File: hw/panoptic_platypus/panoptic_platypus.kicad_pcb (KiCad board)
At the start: 2 copper layers, 127.4 x 73 mm, 206 parts, among them J1 Conn_Coaxial, J2 Conn_Coaxial, J3 Conn_Coaxial, J4 Conn_Coaxial, T1 MABA-011082, T2 MABA-011082, T3 MABA-011082, T4 MABA-011082, U1 MAX2851, U10 ECP5_5G_25_CABGA381, U2 LTC5510, U3 LTC5510, U4 LTC5510, U5 LTC5510, U6 AD9268, U7 AD9268, U8 AD9268, U9 AD9268

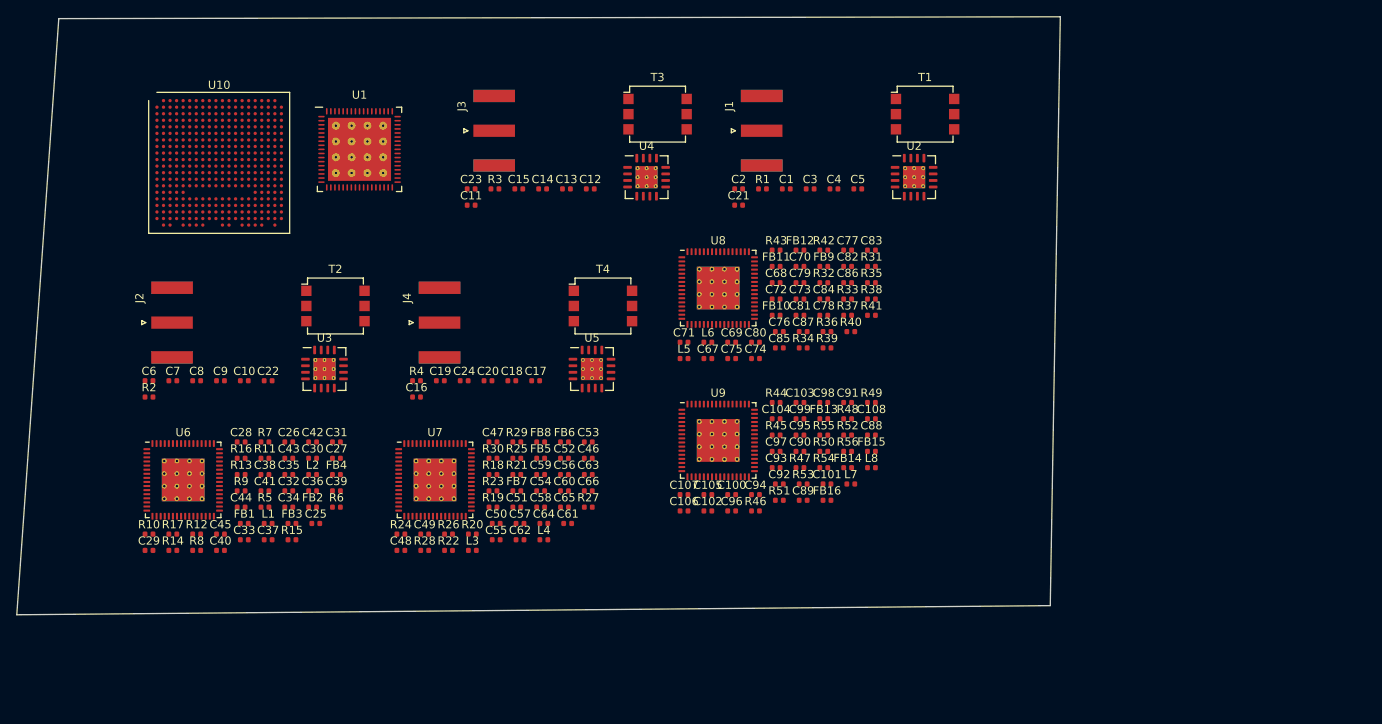
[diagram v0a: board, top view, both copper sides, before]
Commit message: Added LO Generator, fixed some smybols
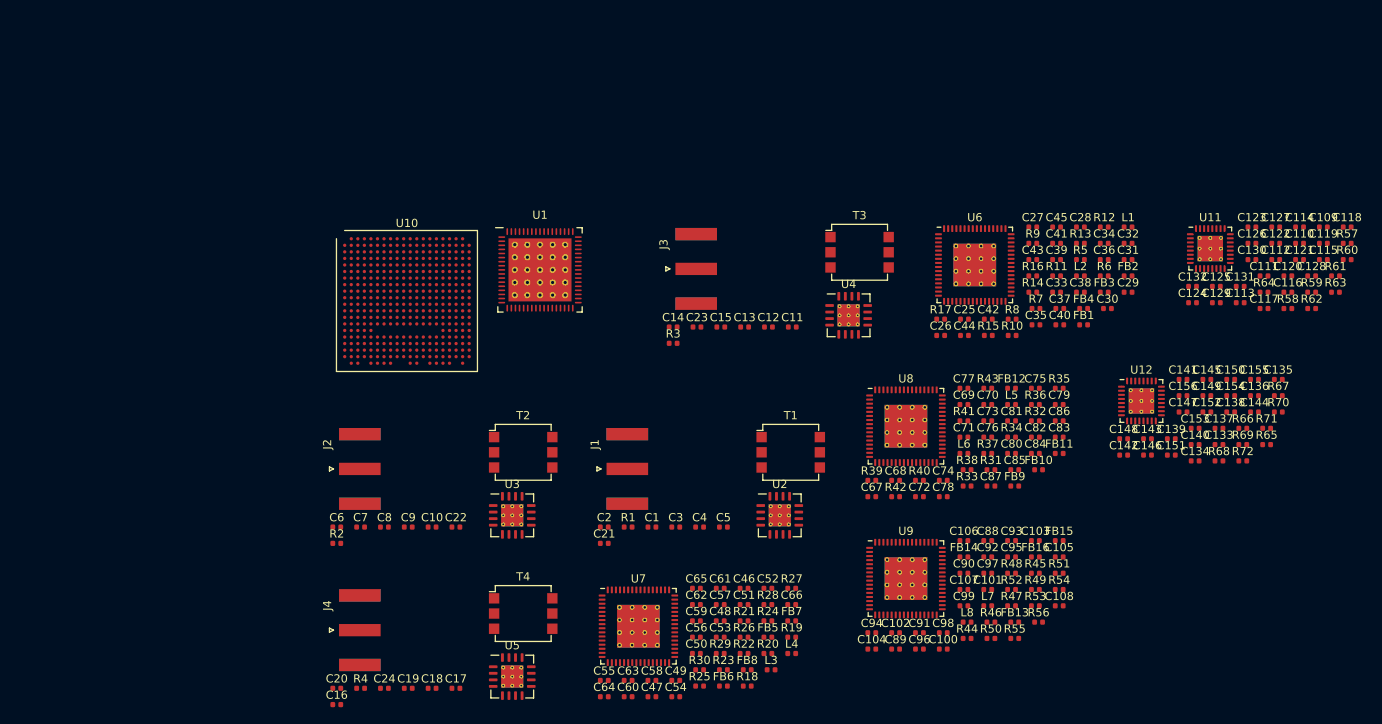
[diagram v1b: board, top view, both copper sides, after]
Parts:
- added C109: 100p, Capacitor_SMD:C_0402_1005Metric, F.Cu at (210.1, 70.8)
- added C110: 100p, Capacitor_SMD:C_0402_1005Metric, F.Cu at (207.2, 72.8)
- added C111: 100p, Capacitor_SMD:C_0402_1005Metric, F.Cu at (202.9, 76.8)
- added C112: 100p, Capacitor_SMD:C_0402_1005Metric, F.Cu at (204.3, 74.8)
- added C113: 0.01u, Capacitor_SMD:C_0402_1005Metric, F.Cu at (200.0, 80.0)
- added C114: 0.01u, Capacitor_SMD:C_0402_1005Metric, F.Cu at (207.2, 70.8)
- added C115: 0.1u, Capacitor_SMD:C_0402_1005Metric, F.Cu at (210.1, 74.8)
- added C116: 100p, Capacitor_SMD:C_0402_1005Metric, F.Cu at (205.8, 78.8)
- added C117: 1u, Capacitor_SMD:C_0402_1005Metric, F.Cu at (202.9, 80.8)
- added C118: 0.1u, Capacitor_SMD:C_0402_1005Metric, F.Cu at (213.0, 70.8)
- added C119: 1u, Capacitor_SMD:C_0402_1005Metric, F.Cu at (210.1, 72.8)
- added C120: 820p, Capacitor_SMD:C_0402_1005Metric, F.Cu at (205.8, 76.8)
- added C121: 100p, Capacitor_SMD:C_0402_1005Metric, F.Cu at (207.2, 74.8)
- added C122: 0.1u, Capacitor_SMD:C_0402_1005Metric, F.Cu at (204.3, 72.8)
- added C123: 0.012u, Capacitor_SMD:C_0402_1005Metric, F.Cu at (201.4, 70.8)
- added C124: 0.1u, Capacitor_SMD:C_0402_1005Metric, F.Cu at (194.1, 80.0)
- added C125: 100p, Capacitor_SMD:C_0402_1005Metric, F.Cu at (197.0, 78.1)
- added C126: 1u, Capacitor_SMD:C_0402_1005Metric, F.Cu at (201.4, 72.8)
- added C127: 0.1u, Capacitor_SMD:C_0402_1005Metric, F.Cu at (204.3, 70.8)
- added C128: 100p, Capacitor_SMD:C_0402_1005Metric, F.Cu at (208.7, 76.8)
- added C129: 0.1u, Capacitor_SMD:C_0402_1005Metric, F.Cu at (197.0, 80.0)
- added C130: 100p, Capacitor_SMD:C_0402_1005Metric, F.Cu at (201.4, 74.8)
- added C131: 0.1u, Capacitor_SMD:C_0402_1005Metric, F.Cu at (200.0, 78.1)
- added C132: 100p, Capacitor_SMD:C_0402_1005Metric, F.Cu at (194.1, 78.1)
- added C133: 100p, Capacitor_SMD:C_0402_1005Metric, F.Cu at (197.4, 97.4)
- added C134: 100p, Capacitor_SMD:C_0402_1005Metric, F.Cu at (194.5, 99.4)
- added C135: 100p, Capacitor_SMD:C_0402_1005Metric, F.Cu at (204.6, 89.4)
- added C136: 100p, Capacitor_SMD:C_0402_1005Metric, F.Cu at (201.7, 91.4)
- added C137: 0.01u, Capacitor_SMD:C_0402_1005Metric, F.Cu at (197.4, 95.4)
- added C138: 0.01u, Capacitor_SMD:C_0402_1005Metric, F.Cu at (198.8, 93.4)
- added C139: 0.1u, Capacitor_SMD:C_0402_1005Metric, F.Cu at (191.5, 96.7)
- added C140: 100p, Capacitor_SMD:C_0402_1005Metric, F.Cu at (194.5, 97.4)
- added C141: 1u, Capacitor_SMD:C_0402_1005Metric, F.Cu at (193.0, 89.4)
- added C142: 0.1u, Capacitor_SMD:C_0402_1005Metric, F.Cu at (185.7, 98.7)
- added C143: 1u, Capacitor_SMD:C_0402_1005Metric, F.Cu at (188.6, 96.7)
- added C144: 820p, Capacitor_SMD:C_0402_1005Metric, F.Cu at (201.7, 93.4)
- added C145: 100p, Capacitor_SMD:C_0402_1005Metric, F.Cu at (195.9, 89.4)
- added C146: 0.1u, Capacitor_SMD:C_0402_1005Metric, F.Cu at (188.6, 98.7)
- added C147: 0.012u, Capacitor_SMD:C_0402_1005Metric, F.Cu at (193.0, 93.4)
- added C148: 0.1u, Capacitor_SMD:C_0402_1005Metric, F.Cu at (185.7, 96.7)
- added C149: 100p, Capacitor_SMD:C_0402_1005Metric, F.Cu at (195.9, 91.4)
- added C150: 1u, Capacitor_SMD:C_0402_1005Metric, F.Cu at (198.8, 89.4)
- added C151: 0.1u, Capacitor_SMD:C_0402_1005Metric, F.Cu at (191.5, 98.7)
- added C152: 100p, Capacitor_SMD:C_0402_1005Metric, F.Cu at (195.9, 93.4)
- added C153: 0.1u, Capacitor_SMD:C_0402_1005Metric, F.Cu at (194.5, 95.4)
- added C154: 100p, Capacitor_SMD:C_0402_1005Metric, F.Cu at (198.8, 91.4)
- added C155: 0.1u, Capacitor_SMD:C_0402_1005Metric, F.Cu at (201.7, 89.4)
- added C156: 100p, Capacitor_SMD:C_0402_1005Metric, F.Cu at (193.0, 91.4)
- added R57: 50, Resistor_SMD:R_0402_1005Metric, F.Cu at (213.0, 72.8)
- added R58: 50, Resistor_SMD:R_0402_1005Metric, F.Cu at (205.8, 80.8)
- added R59: 50, Resistor_SMD:R_0402_1005Metric, F.Cu at (208.7, 78.8)
- added R60: 50, Resistor_SMD:R_0402_1005Metric, F.Cu at (213.0, 74.8)
- added R61: 90.9, Resistor_SMD:R_0402_1005Metric, F.Cu at (211.6, 76.8)
- added R62: 30.1, Resistor_SMD:R_0402_1005Metric, F.Cu at (208.7, 80.8)
- added R63: 240, Resistor_SMD:R_0402_1005Metric, F.Cu at (211.6, 78.8)
- added R64: 5.1k, Resistor_SMD:R_0402_1005Metric, F.Cu at (202.9, 78.8)
- added R65: 50, Resistor_SMD:R_0402_1005Metric, F.Cu at (203.2, 97.4)
- added R66: 50, Resistor_SMD:R_0402_1005Metric, F.Cu at (200.3, 95.4)
- added R67: 50, Resistor_SMD:R_0402_1005Metric, F.Cu at (204.6, 91.4)
- added R68: 50, Resistor_SMD:R_0402_1005Metric, F.Cu at (197.4, 99.4)
- added R69: 90.9, Resistor_SMD:R_0402_1005Metric, F.Cu at (200.3, 97.4)
- added R70: 30.1, Resistor_SMD:R_0402_1005Metric, F.Cu at (204.6, 93.4)
- added R71: 240, Resistor_SMD:R_0402_1005Metric, F.Cu at (203.2, 95.4)
- added R72: 5.1k, Resistor_SMD:R_0402_1005Metric, F.Cu at (200.3, 99.4)
- added U11: MAX2871, Package_DFN_QFN:TQFN-32-1EP_5x5mm_P0.5mm_EP3.1x3.1mm_ThermalVias, F.Cu at (196.3, 73.4)
- added U12: MAX2871, Package_DFN_QFN:TQFN-32-1EP_5x5mm_P0.5mm_EP3.1x3.1mm_ThermalVias, F.Cu at (187.9, 92.0)
- U1: footprint dknueppe:TQFN-68_EP_10x10_Pitch0.5mm -> dknueppe:TQFN-68_EP_10x10_Pitch0.5mm_EP7.7mmx7.7mm_ThermalVias
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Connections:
- net /Analog_Backend/CLK+ renamed /ADC Path2/CLK+
- net /Analog_Backend/CLK- renamed /ADC Path2/CLK-
- net /Analog_Backend/CSB renamed /ADC Path2/CSB
- net /Analog_Backend/DCO_I renamed /ADC Path2/DCO_I
- net /Analog_Backend/DCO_Q renamed /ADC Path2/DCO_Q
- net /Analog_Backend/I_IN+ renamed /ADC Path2/I_IN+
- net /Analog_Backend/I_IN- renamed /ADC Path2/I_IN-
- net /Analog_Backend/I_OUT0 renamed /ADC Path2/I_OUT0
- net /Analog_Backend/I_OUT1 renamed /ADC Path2/I_OUT1
- net /Analog_Backend/I_OUT10 renamed /ADC Path2/I_OUT10
- net /Analog_Backend/I_OUT11 renamed /ADC Path2/I_OUT11
- net /Analog_Backend/I_OUT12 renamed /ADC Path2/I_OUT12
- net /Analog_Backend/I_OUT13 renamed /ADC Path2/I_OUT13
- net /Analog_Backend/I_OUT14 renamed /ADC Path2/I_OUT14
- net /Analog_Backend/I_OUT15 renamed /ADC Path2/I_OUT15
- net /Analog_Backend/I_OUT2 renamed /ADC Path2/I_OUT2
- net /Analog_Backend/I_OUT3 renamed /ADC Path2/I_OUT3
- net /Analog_Backend/I_OUT4 renamed /ADC Path2/I_OUT4
- net /Analog_Backend/I_OUT5 renamed /ADC Path2/I_OUT5
- net /Analog_Backend/I_OUT6 renamed /ADC Path2/I_OUT6
- net /Analog_Backend/I_OUT7 renamed /ADC Path2/I_OUT7
- net /Analog_Backend/I_OUT8 renamed /ADC Path2/I_OUT8
- net /Analog_Backend/I_OUT9 renamed /ADC Path2/I_OUT9
- net /Analog_Backend/OEB renamed /ADC Path2/OEB
- net /Analog_Backend/OR_I renamed /ADC Path2/OR_I
- net /Analog_Backend/OR_Q renamed /ADC Path2/OR_Q
- net /Analog_Backend/PDWN renamed /ADC Path2/PDWN
- net /Analog_Backend/Q_IN+ renamed /ADC Path2/Q_IN+
- net /Analog_Backend/Q_IN- renamed /ADC Path2/Q_IN-
- net /Analog_Backend/Q_OUT0 renamed /ADC Path2/Q_OUT0
- net /Analog_Backend/Q_OUT1 renamed /ADC Path2/Q_OUT1
- net /Analog_Backend/Q_OUT10 renamed /ADC Path2/Q_OUT10
- net /Analog_Backend/Q_OUT11 renamed /ADC Path2/Q_OUT11
- net /Analog_Backend/Q_OUT12 renamed /ADC Path2/Q_OUT12
- net /Analog_Backend/Q_OUT13 renamed /ADC Path2/Q_OUT13
- net /Analog_Backend/Q_OUT14 renamed /ADC Path2/Q_OUT14
- net /Analog_Backend/Q_OUT15 renamed /ADC Path2/Q_OUT15
- net /Analog_Backend/Q_OUT2 renamed /ADC Path2/Q_OUT2
- net /Analog_Backend/Q_OUT3 renamed /ADC Path2/Q_OUT3
- net /Analog_Backend/Q_OUT4 renamed /ADC Path2/Q_OUT4
- net /Analog_Backend/Q_OUT5 renamed /ADC Path2/Q_OUT5
- net /Analog_Backend/Q_OUT6 renamed /ADC Path2/Q_OUT6
- net /Analog_Backend/Q_OUT7 renamed /ADC Path2/Q_OUT7
- net /Analog_Backend/Q_OUT8 renamed /ADC Path2/Q_OUT8
- net /Analog_Backend/Q_OUT9 renamed /ADC Path2/Q_OUT9
- net /Analog_Backend/SCLK renamed /ADC Path2/SCLK
- net /Analog_Backend/SDIO renamed /ADC Path2/SDIO
- net /Analog_Backend/SYNC renamed /ADC Path2/SYNC
- net /sheet5F973422/CLK+ renamed /ADC Path 3/CLK+
- net /sheet5F973422/CLK- renamed /ADC Path 3/CLK-
- net /sheet5F973422/CSB renamed /ADC Path 3/CSB
- net /sheet5F973422/DCO_I renamed /ADC Path 3/DCO_I
- net /sheet5F973422/DCO_Q renamed /ADC Path 3/DCO_Q
- net /sheet5F973422/I_IN+ renamed /ADC Path 3/I_IN+
- net /sheet5F973422/I_IN- renamed /ADC Path 3/I_IN-
- net /sheet5F973422/I_OUT0 renamed /ADC Path 3/I_OUT0
- net /sheet5F973422/I_OUT1 renamed /ADC Path 3/I_OUT1
- net /sheet5F973422/I_OUT10 renamed /ADC Path 3/I_OUT10
- net /sheet5F973422/I_OUT11 renamed /ADC Path 3/I_OUT11
- net /sheet5F973422/I_OUT12 renamed /ADC Path 3/I_OUT12
- net /sheet5F973422/I_OUT13 renamed /ADC Path 3/I_OUT13
- net /sheet5F973422/I_OUT14 renamed /ADC Path 3/I_OUT14
- net /sheet5F973422/I_OUT15 renamed /ADC Path 3/I_OUT15
- net /sheet5F973422/I_OUT2 renamed /ADC Path 3/I_OUT2
- net /sheet5F973422/I_OUT3 renamed /ADC Path 3/I_OUT3
- net /sheet5F973422/I_OUT4 renamed /ADC Path 3/I_OUT4
- net /sheet5F973422/I_OUT5 renamed /ADC Path 3/I_OUT5
- net /sheet5F973422/I_OUT6 renamed /ADC Path 3/I_OUT6
- net /sheet5F973422/I_OUT7 renamed /ADC Path 3/I_OUT7
- net /sheet5F973422/I_OUT8 renamed /ADC Path 3/I_OUT8
- net /sheet5F973422/I_OUT9 renamed /ADC Path 3/I_OUT9
- net /sheet5F973422/OEB renamed /ADC Path 3/OEB
- net /sheet5F973422/OR_I renamed /ADC Path 3/OR_I
- net /sheet5F973422/OR_Q renamed /ADC Path 3/OR_Q
- net /sheet5F973422/PDWN renamed /ADC Path 3/PDWN
- net /sheet5F973422/Q_IN+ renamed /ADC Path 3/Q_IN+
- net /sheet5F973422/Q_IN- renamed /ADC Path 3/Q_IN-
- net /sheet5F973422/Q_OUT0 renamed /ADC Path 3/Q_OUT0
- net /sheet5F973422/Q_OUT1 renamed /ADC Path 3/Q_OUT1
- net /sheet5F973422/Q_OUT10 renamed /ADC Path 3/Q_OUT10
- net /sheet5F973422/Q_OUT11 renamed /ADC Path 3/Q_OUT11
- net /sheet5F973422/Q_OUT12 renamed /ADC Path 3/Q_OUT12
- net /sheet5F973422/Q_OUT13 renamed /ADC Path 3/Q_OUT13
- net /sheet5F973422/Q_OUT14 renamed /ADC Path 3/Q_OUT14
- net /sheet5F973422/Q_OUT15 renamed /ADC Path 3/Q_OUT15
- net /sheet5F973422/Q_OUT2 renamed /ADC Path 3/Q_OUT2
- net /sheet5F973422/Q_OUT3 renamed /ADC Path 3/Q_OUT3
- net /sheet5F973422/Q_OUT4 renamed /ADC Path 3/Q_OUT4
- net /sheet5F973422/Q_OUT5 renamed /ADC Path 3/Q_OUT5
- net /sheet5F973422/Q_OUT6 renamed /ADC Path 3/Q_OUT6
- net /sheet5F973422/Q_OUT7 renamed /ADC Path 3/Q_OUT7
- net /sheet5F973422/Q_OUT8 renamed /ADC Path 3/Q_OUT8
- net /sheet5F973422/Q_OUT9 renamed /ADC Path 3/Q_OUT9
- net /sheet5F973422/SCLK renamed /ADC Path 3/SCLK
- net /sheet5F973422/SDIO renamed /ADC Path 3/SDIO
- net /sheet5F973422/SYNC renamed /ADC Path 3/SYNC
- net /sheet5F973C28/CLK+ renamed /ADC Path 1/CLK+
- net /sheet5F973C28/CLK- renamed /ADC Path 1/CLK-
- net /sheet5F973C28/CSB renamed /ADC Path 1/CSB
- net /sheet5F973C28/DCO_I renamed /ADC Path 1/DCO_I
- net /sheet5F973C28/DCO_Q renamed /ADC Path 1/DCO_Q
- net /sheet5F973C28/I_IN+ renamed /ADC Path 1/I_IN+
- net /sheet5F973C28/I_IN- renamed /ADC Path 1/I_IN-
- net /sheet5F973C28/I_OUT0 renamed /ADC Path 1/I_OUT0
- net /sheet5F973C28/I_OUT1 renamed /ADC Path 1/I_OUT1
- net /sheet5F973C28/I_OUT10 renamed /ADC Path 1/I_OUT10
- net /sheet5F973C28/I_OUT11 renamed /ADC Path 1/I_OUT11
- net /sheet5F973C28/I_OUT12 renamed /ADC Path 1/I_OUT12
- net /sheet5F973C28/I_OUT13 renamed /ADC Path 1/I_OUT13
- net /sheet5F973C28/I_OUT14 renamed /ADC Path 1/I_OUT14
- net /sheet5F973C28/I_OUT15 renamed /ADC Path 1/I_OUT15
- net /sheet5F973C28/I_OUT2 renamed /ADC Path 1/I_OUT2
- net /sheet5F973C28/I_OUT3 renamed /ADC Path 1/I_OUT3
- net /sheet5F973C28/I_OUT4 renamed /ADC Path 1/I_OUT4
- net /sheet5F973C28/I_OUT5 renamed /ADC Path 1/I_OUT5
- net /sheet5F973C28/I_OUT6 renamed /ADC Path 1/I_OUT6
- net /sheet5F973C28/I_OUT7 renamed /ADC Path 1/I_OUT7
- net /sheet5F973C28/I_OUT8 renamed /ADC Path 1/I_OUT8
- net /sheet5F973C28/I_OUT9 renamed /ADC Path 1/I_OUT9
- net /sheet5F973C28/OEB renamed /ADC Path 1/OEB
- net /sheet5F973C28/OR_I renamed /ADC Path 1/OR_I
- net /sheet5F973C28/OR_Q renamed /ADC Path 1/OR_Q
- net /sheet5F973C28/PDWN renamed /ADC Path 1/PDWN
- net /sheet5F973C28/Q_IN+ renamed /ADC Path 1/Q_IN+
- net /sheet5F973C28/Q_IN- renamed /ADC Path 1/Q_IN-
- net /sheet5F973C28/Q_OUT0 renamed /ADC Path 1/Q_OUT0
- net /sheet5F973C28/Q_OUT1 renamed /ADC Path 1/Q_OUT1
- net /sheet5F973C28/Q_OUT10 renamed /ADC Path 1/Q_OUT10
- net /sheet5F973C28/Q_OUT11 renamed /ADC Path 1/Q_OUT11
- net /sheet5F973C28/Q_OUT12 renamed /ADC Path 1/Q_OUT12
- net /sheet5F973C28/Q_OUT13 renamed /ADC Path 1/Q_OUT13
- net /sheet5F973C28/Q_OUT14 renamed /ADC Path 1/Q_OUT14
- net /sheet5F973C28/Q_OUT15 renamed /ADC Path 1/Q_OUT15
- net /sheet5F973C28/Q_OUT2 renamed /ADC Path 1/Q_OUT2
- net /sheet5F973C28/Q_OUT3 renamed /ADC Path 1/Q_OUT3
- net /sheet5F973C28/Q_OUT4 renamed /ADC Path 1/Q_OUT4
- net /sheet5F973C28/Q_OUT5 renamed /ADC Path 1/Q_OUT5
- net /sheet5F973C28/Q_OUT6 renamed /ADC Path 1/Q_OUT6
- net /sheet5F973C28/Q_OUT7 renamed /ADC Path 1/Q_OUT7
- net /sheet5F973C28/Q_OUT8 renamed /ADC Path 1/Q_OUT8
- net /sheet5F973C28/Q_OUT9 renamed /ADC Path 1/Q_OUT9
- net /sheet5F973C28/SCLK renamed /ADC Path 1/SCLK
- net /sheet5F973C28/SDIO renamed /ADC Path 1/SDIO
- net /sheet5F973C28/SYNC renamed /ADC Path 1/SYNC
- net /sheet5F974D16/CLK+ renamed /ADC Path 4/CLK+
- net /sheet5F974D16/CLK- renamed /ADC Path 4/CLK-
- net /sheet5F974D16/CSB renamed /ADC Path 4/CSB
- net /sheet5F974D16/DCO_I renamed /ADC Path 4/DCO_I
- net /sheet5F974D16/DCO_Q renamed /ADC Path 4/DCO_Q
- net /sheet5F974D16/I_IN+ renamed /ADC Path 4/I_IN+
- net /sheet5F974D16/I_IN- renamed /ADC Path 4/I_IN-
- net /sheet5F974D16/I_OUT0 renamed /ADC Path 4/I_OUT0
- net /sheet5F974D16/I_OUT1 renamed /ADC Path 4/I_OUT1
- net /sheet5F974D16/I_OUT10 renamed /ADC Path 4/I_OUT10
- net /sheet5F974D16/I_OUT11 renamed /ADC Path 4/I_OUT11
- net /sheet5F974D16/I_OUT12 renamed /ADC Path 4/I_OUT12
- net /sheet5F974D16/I_OUT13 renamed /ADC Path 4/I_OUT13
- net /sheet5F974D16/I_OUT14 renamed /ADC Path 4/I_OUT14
- net /sheet5F974D16/I_OUT15 renamed /ADC Path 4/I_OUT15
- net /sheet5F974D16/I_OUT2 renamed /ADC Path 4/I_OUT2
- net /sheet5F974D16/I_OUT3 renamed /ADC Path 4/I_OUT3
- net /sheet5F974D16/I_OUT4 renamed /ADC Path 4/I_OUT4
- net /sheet5F974D16/I_OUT5 renamed /ADC Path 4/I_OUT5
- net /sheet5F974D16/I_OUT6 renamed /ADC Path 4/I_OUT6
- net /sheet5F974D16/I_OUT7 renamed /ADC Path 4/I_OUT7
- net /sheet5F974D16/I_OUT8 renamed /ADC Path 4/I_OUT8
- net /sheet5F974D16/I_OUT9 renamed /ADC Path 4/I_OUT9
- net /sheet5F974D16/OEB renamed /ADC Path 4/OEB
- net /sheet5F974D16/OR_I renamed /ADC Path 4/OR_I
- net /sheet5F974D16/OR_Q renamed /ADC Path 4/OR_Q
- net /sheet5F974D16/PDWN renamed /ADC Path 4/PDWN
- net /sheet5F974D16/Q_IN+ renamed /ADC Path 4/Q_IN+
- net /sheet5F974D16/Q_IN- renamed /ADC Path 4/Q_IN-
- net /sheet5F974D16/Q_OUT0 renamed /ADC Path 4/Q_OUT0
- net /sheet5F974D16/Q_OUT1 renamed /ADC Path 4/Q_OUT1
- net /sheet5F974D16/Q_OUT10 renamed /ADC Path 4/Q_OUT10
- net /sheet5F974D16/Q_OUT11 renamed /ADC Path 4/Q_OUT11
- net /sheet5F974D16/Q_OUT12 renamed /ADC Path 4/Q_OUT12
- net /sheet5F974D16/Q_OUT13 renamed /ADC Path 4/Q_OUT13
- net /sheet5F974D16/Q_OUT14 renamed /ADC Path 4/Q_OUT14
- net /sheet5F974D16/Q_OUT15 renamed /ADC Path 4/Q_OUT15
- net /sheet5F974D16/Q_OUT2 renamed /ADC Path 4/Q_OUT2
- net /sheet5F974D16/Q_OUT3 renamed /ADC Path 4/Q_OUT3
- net /sheet5F974D16/Q_OUT4 renamed /ADC Path 4/Q_OUT4
- net /sheet5F974D16/Q_OUT5 renamed /ADC Path 4/Q_OUT5
- net /sheet5F974D16/Q_OUT6 renamed /ADC Path 4/Q_OUT6
- net /sheet5F974D16/Q_OUT7 renamed /ADC Path 4/Q_OUT7
- net /sheet5F974D16/Q_OUT8 renamed /ADC Path 4/Q_OUT8
- net /sheet5F974D16/Q_OUT9 renamed /ADC Path 4/Q_OUT9
- net /sheet5F974D16/SCLK renamed /ADC Path 4/SCLK
- net /sheet5F974D16/SDIO renamed /ADC Path 4/SDIO
- net /sheet5F974D16/SYNC renamed /ADC Path 4/SYNC
- U1 pad 1: Net-(U1-Pad1) -> GND
- U1 pad 22: Net-(U1-Pad22) -> GND
- U1 pad 44: Net-(U1-Pad44) -> GND
- U1 pad 45: Net-(U1-Pad45) -> GND
- U1 pad 50: Net-(U1-Pad50) -> /LO_Generator 1/REF_CLK_IN
- U1 pad 51: Net-(U1-Pad51) -> /LO_Generator 2/REF_CLK_IN
- U1 pad 69: (no net) -> GND
- U10 pad A10: Net-(U10-PadA10) -> (no net)
- U10 pad A11: Net-(U10-PadA11) -> (no net)
- U10 pad A15: Net-(U10-PadA15) -> (no net)
- U10 pad A2: Net-(U10-PadA2) -> (no net)
- U10 pad A3: Net-(U10-PadA3) -> (no net)
- U10 pad A4: Net-(U10-PadA4) -> (no net)
- U10 pad A5: Net-(U10-PadA5) -> (no net)
- U10 pad A6: Net-(U10-PadA6) -> (no net)
- U10 pad A7: Net-(U10-PadA7) -> (no net)
- U10 pad A8: Net-(U10-PadA8) -> (no net)
- U10 pad A9: Net-(U10-PadA9) -> (no net)
- U10 pad B1: Net-(U10-PadB1) -> (no net)
- U10 pad B10: Net-(U10-PadB10) -> (no net)
- U10 pad B11: Net-(U10-PadB11) -> (no net)
- U10 pad B14: GND -> (no net)
- U10 pad B2: Net-(U10-PadB2) -> (no net)
- U10 pad B3: Net-(U10-PadB3) -> (no net)
- U10 pad B4: Net-(U10-PadB4) -> (no net)
- U10 pad B5: Net-(U10-PadB5) -> (no net)
- U10 pad B6: Net-(U10-PadB6) -> (no net)
- U10 pad B7: GND -> (no net)
- U10 pad B8: Net-(U10-PadB8) -> (no net)
- U10 pad B9: Net-(U10-PadB9) -> (no net)
- U10 pad C1: Net-(U10-PadC1) -> (no net)
- U10 pad C10: Net-(U10-PadC10) -> (no net)
- U10 pad C11: Net-(U10-PadC11) -> (no net)
- U10 pad C19: GND -> (no net)
- U10 pad C2: Net-(U10-PadC2) -> (no net)
- U10 pad C3: Net-(U10-PadC3) -> (no net)
- U10 pad C4: Net-(U10-PadC4) -> (no net)
- U10 pad C5: Net-(U10-PadC5) -> (no net)
- U10 pad C6: Net-(U10-PadC6) -> (no net)
- U10 pad C7: Net-(U10-PadC7) -> (no net)
- U10 pad C8: Net-(U10-PadC8) -> (no net)
- U10 pad C9: Net-(U10-PadC9) -> (no net)
- U10 pad D1: Net-(U10-PadD1) -> (no net)
- U10 pad D10: Net-(U10-PadD10) -> (no net)
- U10 pad D2: Net-(U10-PadD2) -> (no net)
- U10 pad D3: Net-(U10-PadD3) -> (no net)
- U10 pad D4: GND -> (no net)
- U10 pad D5: Net-(U10-PadD5) -> (no net)
- U10 pad D6: Net-(U10-PadD6) -> (no net)
- U10 pad D7: Net-(U10-PadD7) -> (no net)
- U10 pad D8: Net-(U10-PadD8) -> (no net)
- U10 pad D9: Net-(U10-PadD9) -> (no net)
- U10 pad E1: Net-(U10-PadE1) -> (no net)
- U10 pad E10: Net-(U10-PadE10) -> (no net)
- U10 pad E2: Net-(U10-PadE2) -> (no net)
- U10 pad E3: Net-(U10-PadE3) -> (no net)
- U10 pad E4: Net-(U10-PadE4) -> (no net)
- U10 pad E5: Net-(U10-PadE5) -> (no net)
- U10 pad E6: Net-(U10-PadE6) -> (no net)
- U10 pad E7: Net-(U10-PadE7) -> (no net)
- U10 pad E8: Net-(U10-PadE8) -> (no net)
- U10 pad E9: Net-(U10-PadE9) -> (no net)
- U10 pad F10: Net-(U10-PadF10) -> (no net)
- U10 pad F13: GND -> (no net)
- U10 pad F14: GND -> (no net)
- U10 pad F15: Net-(U10-PadF15) -> (no net)
- U10 pad F2: Net-(U10-PadF2) -> (no net)
- U10 pad F3: Net-(U10-PadF3) -> (no net)
- U10 pad F4: Net-(U10-PadF4) -> (no net)
- U10 pad F5: Net-(U10-PadF5) -> (no net)
- U10 pad F6: Net-(U10-PadF6) -> (no net)
- U10 pad F7: GND -> (no net)
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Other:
- board outline removed

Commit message: added power supply, connected up some bits
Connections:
- net Net-(U10-PadA12) renamed /O_OUT_A10
- net Net-(U10-PadA13) renamed /O_OUT_A8
- net Net-(U10-PadA14) renamed /O_OUT_A3
- net Net-(U10-PadB12) renamed /O_OUT_A14
- net Net-(U10-PadB13) renamed /O_OUT_A7
- net Net-(U10-PadC12) renamed /O_OUT_A12
- net Net-(U10-PadC13) renamed /O_OUT_A5
- net Net-(U10-PadC14) renamed /O_OUT_A1
- net Net-(U10-PadD11) renamed /O_OUT_A15
- net Net-(U10-PadD12) renamed /O_OUT_A11
- net Net-(U10-PadD13) renamed /O_OUT_A6
- net Net-(U10-PadD14) renamed /O_OUT_A2
- net Net-(U10-PadE11) renamed /O_OUT_A13
- net Net-(U10-PadE12) renamed /O_OUT_A9
- net Net-(U10-PadE13) renamed /O_OUT_A4
- net Net-(U10-PadE14) renamed /O_OUT_A0
- net Net-(U10-PadL1) renamed /Q_OUT_C9
- net Net-(U10-PadL16) renamed /Q_OUT_B11
- net Net-(U10-PadL17) renamed /Q_OUT_B9
- net Net-(U10-PadL18) renamed /Q_OUT_B10
- net Net-(U10-PadL19) renamed /Q_OUT_B14
- net Net-(U10-PadL2) renamed /Q_OUT_C7
- net Net-(U10-PadL20) renamed /Q_OUT_B15
- net Net-(U10-PadL3) renamed /Q_OUT_C5
- net Net-(U10-PadM1) renamed /Q_OUT_C10
- net Net-(U10-PadM17) renamed /Q_OUT_B5
- net Net-(U10-PadM18) renamed /Q_OUT_B8
- net Net-(U10-PadM19) renamed /Q_OUT_B12
- net Net-(U10-PadM20) renamed /Q_OUT_B13
- net Net-(U10-PadM3) renamed /Q_OUT_C6
- net Net-(U10-PadM4) renamed /Q_OUT_C0
- net Net-(U10-PadN1) renamed /Q_OUT_C11
- net Net-(U10-PadN16) renamed /Q_OUT_B7
- net Net-(U10-PadN17) renamed /Q_OUT_B3
- net Net-(U10-PadN18) renamed /Q_OUT_B6
- net Net-(U10-PadN2) renamed /Q_OUT_C8
- net Net-(U10-PadN3) renamed /Q_OUT_C4
- net Net-(U10-PadN4) renamed /Q_OUT_C1
- net Net-(U10-PadN5) renamed /Q_OUT_C2
- net Net-(U10-PadP1) renamed /Q_OUT_C12
- net Net-(U10-PadP16) renamed /Q_OUT_B1
- net Net-(U10-PadP17) renamed /Q_OUT_B4
- net Net-(U10-PadP2) renamed /Q_OUT_C13
- net Net-(U10-PadP3) renamed /Q_OUT_C14
- net Net-(U10-PadP4) renamed /Q_OUT_C15
- net Net-(U10-PadP5) renamed /Q_OUT_C3
- net Net-(U10-PadR16) renamed /Q_OUT_B2
- net Net-(U10-PadR17) renamed /Q_OUT_B0
- C109 pad 2: /LO_Generator 1/LO_OUT_A- -> /LO_A-
- C110 pad 2: /LO_Generator 1/LO_OUT_A+ -> /LO_A+
- C111 pad 2: /LO_Generator 1/LO_OUT_B- -> /LO_B-
- C112 pad 2: /LO_Generator 1/LO_OUT_B+ -> /LO_B+
- C133 pad 2: /LO_Generator 2/LO_OUT_A- -> /LO_C-
- C134 pad 2: /LO_Generator 2/LO_OUT_A+ -> /LO_C+
- C135 pad 2: /LO_Generator 2/LO_OUT_B- -> /LO_D-
- C136 pad 2: /LO_Generator 2/LO_OUT_B+ -> /LO_D+
- C139 pad 1: /LO_Generator 2/DVCC -> /LO_Generator 1/DVCC
- C140 pad 1: /LO_Generator 2/DVCC -> /LO_Generator 1/DVCC
- C142 pad 1: /LO_Generator 2/DVCC -> /LO_Generator 1/DVCC
- C145 pad 1: /LO_Generator 2/DVCC -> /LO_Generator 1/DVCC
- C148 pad 1: /LO_Generator 2/AVCC -> /LO_Generator 1/AVCC
- C149 pad 1: /LO_Generator 2/AVCC -> /LO_Generator 1/AVCC
- C151 pad 1: /LO_Generator 2/AVCC -> /LO_Generator 1/AVCC
- C152 pad 1: /LO_Generator 2/AVCC -> /LO_Generator 1/AVCC
- C153 pad 1: /LO_Generator 2/AVCC -> /LO_Generator 1/AVCC
- C154 pad 1: /LO_Generator 2/AVCC -> /LO_Generator 1/AVCC
- C155 pad 1: /LO_Generator 2/AVCC -> /LO_Generator 1/AVCC
- C156 pad 1: /LO_Generator 2/AVCC -> /LO_Generator 1/AVCC
- U10 pad A10: (no net) -> Net-(U10-PadA10)
- U10 pad A11: (no net) -> Net-(U10-PadA11)
- U10 pad A15: (no net) -> Net-(U10-PadA15)
- U10 pad A16: Net-(U10-PadA16) -> /I_OUT_A11
- U10 pad A17: Net-(U10-PadA17) -> /I_OUT_A6
- U10 pad A18: Net-(U10-PadA18) -> /I_OUT_A3
- U10 pad A19: Net-(U10-PadA19) -> /I_OUT_A2
- U10 pad A6: (no net) -> Net-(U10-PadA6)
- U10 pad A7: (no net) -> Net-(U10-PadA7)
- U10 pad A8: (no net) -> Net-(U10-PadA8)
- U10 pad A9: (no net) -> Net-(U10-PadA9)
- U10 pad B10: (no net) -> Net-(U10-PadB10)
- U10 pad B11: (no net) -> Net-(U10-PadB11)
- U10 pad B14: (no net) -> GND
- U10 pad B15: Net-(U10-PadB15) -> /I_OUT_A15
- U10 pad B16: Net-(U10-PadB16) -> /I_OUT_A9
- U10 pad B17: Net-(U10-PadB17) -> /I_OUT_A7
- U10 pad B18: Net-(U10-PadB18) -> /I_OUT_A4
- U10 pad B19: Net-(U10-PadB19) -> /I_OUT_A1
- U10 pad B20: Net-(U10-PadB20) -> /I_OUT_A0
- U10 pad B6: (no net) -> Net-(U10-PadB6)
- U10 pad B7: (no net) -> GND
- U10 pad B8: (no net) -> Net-(U10-PadB8)
- U10 pad B9: (no net) -> Net-(U10-PadB9)
- U10 pad C10: (no net) -> Net-(U10-PadC10)
- U10 pad C11: (no net) -> Net-(U10-PadC11)
- U10 pad C15: Net-(U10-PadC15) -> /I_OUT_A13
- U10 pad C16: Net-(U10-PadC16) -> /I_OUT_A10
- U10 pad C17: Net-(U10-PadC17) -> /I_OUT_A5
- U10 pad C18: Net-(U10-PadC18) -> /Q_OUT_D15
- U10 pad C19: (no net) -> GND
- U10 pad C20: Net-(U10-PadC20) -> /I_OUT_D15
- U10 pad C6: (no net) -> Net-(U10-PadC6)
- U10 pad C7: (no net) -> Net-(U10-PadC7)
- U10 pad C8: (no net) -> Net-(U10-PadC8)
- U10 pad C9: (no net) -> Net-(U10-PadC9)
- U10 pad D10: (no net) -> Net-(U10-PadD10)
- U10 pad D15: Net-(U10-PadD15) -> /I_OUT_A14
- U10 pad D16: Net-(U10-PadD16) -> /I_OUT_A8
- U10 pad D17: Net-(U10-PadD17) -> /Q_OUT_D14
- U10 pad D18: Net-(U10-PadD18) -> /Q_OUT_D11
- U10 pad D19: Net-(U10-PadD19) -> /I_OUT_D13
- U10 pad D20: Net-(U10-PadD20) -> /I_OUT_D14
- U10 pad D4: (no net) -> GND
- U10 pad D6: (no net) -> Net-(U10-PadD6)
- U10 pad D7: (no net) -> Net-(U10-PadD7)
- U10 pad D8: (no net) -> Net-(U10-PadD8)
- U10 pad D9: (no net) -> Net-(U10-PadD9)
- U10 pad E10: (no net) -> Net-(U10-PadE10)
- U10 pad E15: Net-(U10-PadE15) -> /I_OUT_A12
- U10 pad E16: Net-(U10-PadE16) -> /Q_OUT_D13
- U10 pad E17: Net-(U10-PadE17) -> /Q_OUT_D9
- U10 pad E18: Net-(U10-PadE18) -> /Q_OUT_D10
- U10 pad E19: Net-(U10-PadE19) -> /I_OUT_D12
- U10 pad E20: Net-(U10-PadE20) -> /I_OUT_D11
- U10 pad E6: (no net) -> Net-(U10-PadE6)
- U10 pad E7: (no net) -> Net-(U10-PadE7)
- U10 pad E8: (no net) -> Net-(U10-PadE8)
- U10 pad E9: (no net) -> Net-(U10-PadE9)
- U10 pad F1: Net-(U10-PadF1) -> /I_OUT_C2
- U10 pad F10: (no net) -> Net-(U10-PadF10)
- U10 pad F13: (no net) -> GND
- U10 pad F14: (no net) -> GND
- U10 pad F15: (no net) -> VCC
- U10 pad F16: Net-(U10-PadF16) -> /Q_OUT_D12
- U10 pad F17: Net-(U10-PadF17) -> /Q_OUT_D7
- U10 pad F18: Net-(U10-PadF18) -> /Q_OUT_D8
- U10 pad F19: Net-(U10-PadF19) -> /I_OUT_D9
- U10 pad F20: Net-(U10-PadF20) -> /I_OUT_D10
- U10 pad F6: (no net) -> VCC
- U10 pad F7: (no net) -> GND
- U10 pad F8: (no net) -> GND
- U10 pad F9: (no net) -> Net-(U10-PadF9)
- U10 pad G1: Net-(U10-PadG1) -> /I_OUT_C3
- U10 pad G10: (no net) -> GND
- U10 pad G11: (no net) -> GND
- U10 pad G12: (no net) -> GND
- U10 pad G13: (no net) -> GND
- U10 pad G14: (no net) -> GND
- U10 pad G15: (no net) -> GND
- U10 pad G16: Net-(U10-PadG16) -> /Q_OUT_D6
- U10 pad G17: (no net) -> GND
- U10 pad G18: Net-(U10-PadG18) -> /Q_OUT_D5
- U10 pad G19: Net-(U10-PadG19) -> /I_OUT_D7
- U10 pad G2: Net-(U10-PadG2) -> /I_OUT_C0
- U10 pad G20: Net-(U10-PadG20) -> /I_OUT_D8
- U10 pad G4: (no net) -> GND
- U10 pad G6: (no net) -> GND
- U10 pad G7: (no net) -> GND
- U10 pad G8: (no net) -> GND
- U10 pad G9: (no net) -> GND
- U10 pad H1: Net-(U10-PadH1) -> /I_OUT_C9
- U10 pad H10: (no net) -> VCC
- U10 pad H11: (no net) -> VCC
- U10 pad H12: (no net) -> VCC
- U10 pad H13: (no net) -> VCC
- U10 pad H16: Net-(U10-PadH16) -> /Q_OUT_D4
- U10 pad H17: Net-(U10-PadH17) -> /Q_OUT_D1
- U10 pad H18: Net-(U10-PadH18) -> /Q_OUT_D3
- U10 pad H19: (no net) -> GND
- U10 pad H2: Net-(U10-PadH2) -> /I_OUT_C1
- U10 pad H20: Net-(U10-PadH20) -> /I_OUT_D5
- U10 pad H8: (no net) -> VCC
- U10 pad H9: (no net) -> VCC
- U10 pad J1: Net-(U10-PadJ1) -> /I_OUT_C10
- U10 pad J10: (no net) -> GND
- U10 pad J11: (no net) -> GND
- U10 pad J12: (no net) -> GND
- U10 pad J13: (no net) -> VCC
- U10 pad J14: (no net) -> GND
- U10 pad J16: Net-(U10-PadJ16) -> /Q_OUT_D0
- U10 pad J17: Net-(U10-PadJ17) -> /Q_OUT_D2
- U10 pad J18: Net-(U10-PadJ18) -> /I_OUT_D6
- U10 pad J19: Net-(U10-PadJ19) -> /I_OUT_D3
- U10 pad J2: (no net) -> GND
- U10 pad J20: Net-(U10-PadJ20) -> /I_OUT_D2
- U10 pad J3: Net-(U10-PadJ3) -> /I_OUT_C5
- U10 pad J4: Net-(U10-PadJ4) -> /I_OUT_C4
- U10 pad J5: Net-(U10-PadJ5) -> /I_OUT_C6
- U10 pad J7: (no net) -> GND
- U10 pad J8: (no net) -> VCC
- U10 pad J9: (no net) -> GND
- U10 pad K1: Net-(U10-PadK1) -> /I_OUT_C11
- U10 pad K10: (no net) -> GND
- U10 pad K11: (no net) -> GND
- U10 pad K12: (no net) -> GND
- U10 pad K13: (no net) -> VCC
- U10 pad K14: (no net) -> GND
- U10 pad K15: (no net) -> GND
- U10 pad K16: (no net) -> Net-(U10-PadK16)
- U10 pad K17: (no net) -> Net-(U10-PadK17)
- U10 pad K18: Net-(U10-PadK18) -> /I_OUT_D4
- U10 pad K19: Net-(U10-PadK19) -> /I_OUT_D1
- U10 pad K2: Net-(U10-PadK2) -> /I_OUT_C8
- U10 pad K20: Net-(U10-PadK20) -> /I_OUT_D0
- U10 pad K3: Net-(U10-PadK3) -> /I_OUT_C7
- U10 pad K4: Net-(U10-PadK4) -> /I_OUT_C12
- U10 pad K5: Net-(U10-PadK5) -> /I_OUT_C14
- U10 pad K6: (no net) -> GND
- U10 pad K7: (no net) -> GND
- U10 pad K8: (no net) -> VCC
- U10 pad K9: (no net) -> GND
- U10 pad L10: (no net) -> GND
- U10 pad L11: (no net) -> GND
- U10 pad L12: (no net) -> GND
- U10 pad L13: (no net) -> VCC
- U10 pad L4: Net-(U10-PadL4) -> /I_OUT_C13
- U10 pad L5: Net-(U10-PadL5) -> /I_OUT_C15
- U10 pad L8: (no net) -> VCC
- U10 pad L9: (no net) -> GND
- U10 pad M10: (no net) -> GND
- U10 pad M11: (no net) -> GND
- U10 pad M12: (no net) -> GND
- U10 pad M13: (no net) -> VCC
- U10 pad M14: (no net) -> GND
- U10 pad M16: (no net) -> GND
- U10 pad M2: (no net) -> GND
- U10 pad M5: (no net) -> Net-(U10-PadM5)
- U10 pad M7: (no net) -> GND
- U10 pad M8: (no net) -> VCC
- U10 pad M9: (no net) -> GND
- U10 pad N10: (no net) -> VCC
- U10 pad N11: (no net) -> VCC
- U10 pad N12: (no net) -> VCC
- U10 pad N13: (no net) -> VCC
- U10 pad N14: (no net) -> GND
- U10 pad N15: (no net) -> GND
- U10 pad N19: Net-(U10-PadN19) -> /I_OUT_B15
- U10 pad N20: Net-(U10-PadN20) -> /I_OUT_B13
- U10 pad N6: (no net) -> GND
- U10 pad N7: (no net) -> GND
- U10 pad N8: (no net) -> VCC
- U10 pad N9: (no net) -> VCC
- U10 pad P10: (no net) -> Net-(U10-PadP10)
- U10 pad P11: (no net) -> GND
- U10 pad P12: (no net) -> GND
- U10 pad P13: (no net) -> GND
- U10 pad P14: (no net) -> GND
- U10 pad P15: (no net) -> VCC
- U10 pad P18: Net-(U10-PadP18) -> /I_OUT_B12
- U10 pad P19: Net-(U10-PadP19) -> /I_OUT_B14
- U10 pad P20: Net-(U10-PadP20) -> /I_OUT_B11
- U10 pad P6: (no net) -> VCC
- U10 pad P7: (no net) -> GND
- U10 pad P8: (no net) -> GND
- U10 pad P9: (no net) -> Net-(U10-PadP9)
- U10 pad R1: (no net) -> Net-(U10-PadR1)
- U10 pad R18: Net-(U10-PadR18) -> /I_OUT_B5
- U10 pad R19: (no net) -> GND
- U10 pad R2: (no net) -> Net-(U10-PadR2)
- U10 pad R20: Net-(U10-PadR20) -> /I_OUT_B9
- U10 pad R3: (no net) -> Net-(U10-PadR3)
- U10 pad R4: (no net) -> Net-(U10-PadR4)
- U10 pad R5: (no net) -> Net-(U10-PadR5)
- U10 pad T1: (no net) -> Net-(U10-PadT1)
- U10 pad T10: (no net) -> VCC
- U10 pad T11: (no net) -> Net-(U10-PadT11)
- U10 pad T12: (no net) -> Net-(U10-PadT12)
- U10 pad T13: (no net) -> Net-(U10-PadT13)
- U10 pad T14: (no net) -> Net-(U10-PadT14)
- U10 pad T15: (no net) -> Net-(U10-PadT15)
- U10 pad T16: (no net) -> Net-(U10-PadT16)
- U10 pad T17: Net-(U10-PadT17) -> /I_OUT_B0
- U10 pad T18: Net-(U10-PadT18) -> /I_OUT_B4
- U10 pad T19: Net-(U10-PadT19) -> /I_OUT_B7
- U10 pad T2: (no net) -> Net-(U10-PadT2)
- U10 pad T20: Net-(U10-PadT20) -> /I_OUT_B10
- U10 pad T3: (no net) -> Net-(U10-PadT3)
- U10 pad T4: (no net) -> Net-(U10-PadT4)
- U10 pad T5: (no net) -> Net-(U10-PadT5)
- U10 pad T6: (no net) -> VCC
- U10 pad T7: (no net) -> VCC
- U10 pad T8: (no net) -> VCC
- U10 pad T9: (no net) -> VCC
- U10 pad U1: (no net) -> Net-(U10-PadU1)
- U10 pad U10: (no net) -> GND
- U10 pad U11: (no net) -> GND
- U10 pad U12: (no net) -> GND
- U10 pad U13: (no net) -> GND
- U10 pad U14: (no net) -> GND
- U10 pad U15: (no net) -> Net-(U10-PadU15)
- U10 pad U16: Net-(U10-PadU16) -> /I_OUT_B1
- U10 pad U17: Net-(U10-PadU17) -> /I_OUT_B2
- U10 pad U18: Net-(U10-PadU18) -> /I_OUT_B3
- U10 pad U19: Net-(U10-PadU19) -> /I_OUT_B6
- U10 pad U2: (no net) -> Net-(U10-PadU2)
- U10 pad U20: Net-(U10-PadU20) -> /I_OUT_B8
- U10 pad U3: (no net) -> Net-(U10-PadU3)
- U10 pad U4: (no net) -> Net-(U10-PadU4)
- U10 pad U5: (no net) -> Net-(U10-PadU5)
- U10 pad U6: (no net) -> VCC
- U10 pad U7: (no net) -> GND
- U10 pad U8: (no net) -> GND
- U10 pad U9: (no net) -> GND
- U10 pad V1: (no net) -> Net-(U10-PadV1)
- U10 pad V10: (no net) -> VCC
- U10 pad V11: (no net) -> VCC
- U10 pad V12: (no net) -> GND
- U10 pad V13: (no net) -> GND
- U10 pad V14: (no net) -> GND
- U10 pad V15: (no net) -> GND
- U10 pad V16: (no net) -> GND
- U10 pad V17: (no net) -> Net-(U10-PadV17)
- U10 pad V18: (no net) -> Net-(U10-PadV18)
- U10 pad V19: (no net) -> GND
- U10 pad V2: (no net) -> Net-(U10-PadV2)
- U10 pad V20: (no net) -> GND
- U10 pad V3: (no net) -> Net-(U10-PadV3)
- U10 pad V4: (no net) -> Net-(U10-PadV4)
- U10 pad V5: (no net) -> GND
- U10 pad V6: (no net) -> GND
- U10 pad V7: (no net) -> GND
- U10 pad V8: (no net) -> GND
- U10 pad V9: (no net) -> GND
- U10 pad W1: (no net) -> Net-(U10-PadW1)
- U10 pad W10: (no net) -> Net-(U10-PadW10)
- U10 pad W11: (no net) -> Net-(U10-PadW11)
- U10 pad W12: (no net) -> GND
- U10 pad W13: (no net) -> Net-(U10-PadW13)
- U10 pad W14: (no net) -> Net-(U10-PadW14)
- U10 pad W15: (no net) -> GND
- U10 pad W16: (no net) -> GND
- U10 pad W17: (no net) -> Net-(U10-PadW17)
- U10 pad W18: (no net) -> Net-(U10-PadW18)
- U10 pad W19: (no net) -> GND
- U10 pad W2: (no net) -> Net-(U10-PadW2)
- U10 pad W20: (no net) -> Net-(U10-PadW20)
- U10 pad W3: (no net) -> Net-(U10-PadW3)
- U10 pad W4: (no net) -> Net-(U10-PadW4)
- U10 pad W5: (no net) -> Net-(U10-PadW5)
- U10 pad W6: (no net) -> GND
- U10 pad W7: (no net) -> GND
- U10 pad W8: (no net) -> Net-(U10-PadW8)
- U10 pad W9: (no net) -> Net-(U10-PadW9)
- U10 pad Y11: (no net) -> Net-(U10-PadY11)
- U10 pad Y12: (no net) -> Net-(U10-PadY12)
- U10 pad Y14: (no net) -> Net-(U10-PadY14)
- U10 pad Y15: (no net) -> Net-(U10-PadY15)
- U10 pad Y16: (no net) -> Net-(U10-PadY16)
- U10 pad Y17: (no net) -> Net-(U10-PadY17)
- U10 pad Y19: (no net) -> Net-(U10-PadY19)
- U10 pad Y2: (no net) -> Net-(U10-PadY2)
- U10 pad Y3: (no net) -> Net-(U10-PadY3)
- U10 pad Y5: (no net) -> Net-(U10-PadY5)
- U10 pad Y6: (no net) -> Net-(U10-PadY6)
- U10 pad Y7: (no net) -> Net-(U10-PadY7)
- U10 pad Y8: (no net) -> Net-(U10-PadY8)
- U12 pad 10: /LO_Generator 2/AVCC -> /LO_Generator 1/AVCC
- U12 pad 16: /LO_Generator 2/AVCC -> /LO_Generator 1/AVCC
- U12 pad 17: /LO_Generator 2/AVCC -> /LO_Generator 1/AVCC
- U12 pad 28: /LO_Generator 2/DVCC -> /LO_Generator 1/DVCC
- U12 pad 32: /LO_Generator 2/DVCC -> /LO_Generator 1/DVCC
- U12 pad 6: /LO_Generator 2/AVCC -> /LO_Generator 1/AVCC
- U2 pad 14: /Input and Mixer 1/LO- -> /LO_A-
- U2 pad 15: /Input and Mixer 1/LO+ -> /LO_A+
- U3 pad 14: /Input and Mixer 2/LO- -> /LO_B-
- U3 pad 15: /Input and Mixer 2/LO+ -> /LO_B+
- U4 pad 14: /Input and Mixer 3/LO- -> /LO_C-
- U4 pad 15: /Input and Mixer 3/LO+ -> /LO_C+
- U5 pad 14: /Input and Mixer 4/LO- -> /LO_D-
- U5 pad 15: /Input and Mixer 4/LO+ -> /LO_D+
- U6 pad 25: /ADC Path2/I_OUT0 -> /I_OUT_B0
- U6 pad 26: /ADC Path2/I_OUT1 -> /I_OUT_B1
- U6 pad 27: /ADC Path2/I_OUT2 -> /I_OUT_B2
- U6 pad 29: /ADC Path2/I_OUT3 -> /I_OUT_B3
- U6 pad 30: /ADC Path2/I_OUT4 -> /I_OUT_B4
- U6 pad 31: /ADC Path2/I_OUT5 -> /I_OUT_B5
- U6 pad 32: /ADC Path2/I_OUT6 -> /I_OUT_B6
- U6 pad 33: /ADC Path2/I_OUT7 -> /I_OUT_B7
- U6 pad 34: /ADC Path2/I_OUT8 -> /I_OUT_B8
- U6 pad 35: /ADC Path2/I_OUT9 -> /I_OUT_B9
- U6 pad 36: /ADC Path2/I_OUT10 -> /I_OUT_B10
- U6 pad 38: /ADC Path2/I_OUT11 -> /I_OUT_B11
- U6 pad 39: /ADC Path2/I_OUT12 -> /I_OUT_B12
- U6 pad 40: /ADC Path2/I_OUT13 -> /I_OUT_B13
- U6 pad 41: /ADC Path2/I_OUT14 -> /I_OUT_B14
- U6 pad 42: /ADC Path2/I_OUT15 -> /I_OUT_B15
- U7 pad 25: /ADC Path 3/I_OUT0 -> /I_OUT_C0
- U7 pad 26: /ADC Path 3/I_OUT1 -> /I_OUT_C1
- U7 pad 27: /ADC Path 3/I_OUT2 -> /I_OUT_C2
- U7 pad 29: /ADC Path 3/I_OUT3 -> /I_OUT_C3
- U7 pad 30: /ADC Path 3/I_OUT4 -> /I_OUT_C4
- U7 pad 31: /ADC Path 3/I_OUT5 -> /I_OUT_C5
- U7 pad 32: /ADC Path 3/I_OUT6 -> /I_OUT_C6
- U7 pad 33: /ADC Path 3/I_OUT7 -> /I_OUT_C7
- U7 pad 34: /ADC Path 3/I_OUT8 -> /I_OUT_C8
- U7 pad 35: /ADC Path 3/I_OUT9 -> /I_OUT_C9
- U7 pad 36: /ADC Path 3/I_OUT10 -> /I_OUT_C10
- U7 pad 38: /ADC Path 3/I_OUT11 -> /I_OUT_C11
- U7 pad 39: /ADC Path 3/I_OUT12 -> /I_OUT_C12
- U7 pad 40: /ADC Path 3/I_OUT13 -> /I_OUT_C13
- U7 pad 41: /ADC Path 3/I_OUT14 -> /I_OUT_C14
- U7 pad 42: /ADC Path 3/I_OUT15 -> /I_OUT_C15
- U8 pad 25: /ADC Path 1/I_OUT0 -> /I_OUT_A0
- U8 pad 26: /ADC Path 1/I_OUT1 -> /I_OUT_A1
- U8 pad 27: /ADC Path 1/I_OUT2 -> /I_OUT_A2
- U8 pad 29: /ADC Path 1/I_OUT3 -> /I_OUT_A3
- U8 pad 30: /ADC Path 1/I_OUT4 -> /I_OUT_A4
- U8 pad 31: /ADC Path 1/I_OUT5 -> /I_OUT_A5
- U8 pad 32: /ADC Path 1/I_OUT6 -> /I_OUT_A6
- U8 pad 33: /ADC Path 1/I_OUT7 -> /I_OUT_A7
- U8 pad 34: /ADC Path 1/I_OUT8 -> /I_OUT_A8
- U8 pad 35: /ADC Path 1/I_OUT9 -> /I_OUT_A9
- U8 pad 36: /ADC Path 1/I_OUT10 -> /I_OUT_A10
- U8 pad 38: /ADC Path 1/I_OUT11 -> /I_OUT_A11
- U8 pad 39: /ADC Path 1/I_OUT12 -> /I_OUT_A12
- U8 pad 40: /ADC Path 1/I_OUT13 -> /I_OUT_A13
- U8 pad 41: /ADC Path 1/I_OUT14 -> /I_OUT_A14
- U8 pad 42: /ADC Path 1/I_OUT15 -> /I_OUT_A15
- U9 pad 11: /ADC Path 4/Q_OUT6 -> /Q_OUT_D6
- U9 pad 12: /ADC Path 4/Q_OUT7 -> /Q_OUT_D7
- U9 pad 13: /ADC Path 4/Q_OUT8 -> /Q_OUT_D8
- U9 pad 14: /ADC Path 4/Q_OUT9 -> /Q_OUT_D9
- U9 pad 15: /ADC Path 4/Q_OUT10 -> /Q_OUT_D10
- U9 pad 16: /ADC Path 4/Q_OUT11 -> /Q_OUT_D11
- U9 pad 17: /ADC Path 4/Q_OUT12 -> /Q_OUT_D12
- U9 pad 18: /ADC Path 4/Q_OUT13 -> /Q_OUT_D13
- U9 pad 20: /ADC Path 4/Q_OUT14 -> /Q_OUT_D14
- U9 pad 21: /ADC Path 4/Q_OUT15 -> /Q_OUT_D15
- U9 pad 25: /ADC Path 4/I_OUT0 -> /I_OUT_D0
- U9 pad 26: /ADC Path 4/I_OUT1 -> /I_OUT_D1
- U9 pad 27: /ADC Path 4/I_OUT2 -> /I_OUT_D2
- U9 pad 29: /ADC Path 4/I_OUT3 -> /I_OUT_D3
- U9 pad 30: /ADC Path 4/I_OUT4 -> /I_OUT_D4
- U9 pad 31: /ADC Path 4/I_OUT5 -> /I_OUT_D5
- U9 pad 32: /ADC Path 4/I_OUT6 -> /I_OUT_D6
- U9 pad 33: /ADC Path 4/I_OUT7 -> /I_OUT_D7
- U9 pad 34: /ADC Path 4/I_OUT8 -> /I_OUT_D8
- U9 pad 35: /ADC Path 4/I_OUT9 -> /I_OUT_D9
- U9 pad 36: /ADC Path 4/I_OUT10 -> /I_OUT_D10
- U9 pad 38: /ADC Path 4/I_OUT11 -> /I_OUT_D11
- U9 pad 39: /ADC Path 4/I_OUT12 -> /I_OUT_D12
- U9 pad 4: /ADC Path 4/Q_OUT0 -> /Q_OUT_D0
- U9 pad 40: /ADC Path 4/I_OUT13 -> /I_OUT_D13
- U9 pad 41: /ADC Path 4/I_OUT14 -> /I_OUT_D14
- U9 pad 42: /ADC Path 4/I_OUT15 -> /I_OUT_D15
- U9 pad 5: /ADC Path 4/Q_OUT1 -> /Q_OUT_D1
- U9 pad 6: /ADC Path 4/Q_OUT2 -> /Q_OUT_D2
- U9 pad 7: /ADC Path 4/Q_OUT3 -> /Q_OUT_D3
- U9 pad 8: /ADC Path 4/Q_OUT4 -> /Q_OUT_D4
- U9 pad 9: /ADC Path 4/Q_OUT5 -> /Q_OUT_D5
